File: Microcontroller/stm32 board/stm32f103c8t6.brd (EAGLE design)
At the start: 100 x 80 mm, 19 parts, among them J2 796136-1, Q1 8MHz, U1 STM32F103C8T6, X1 32.768KHZ

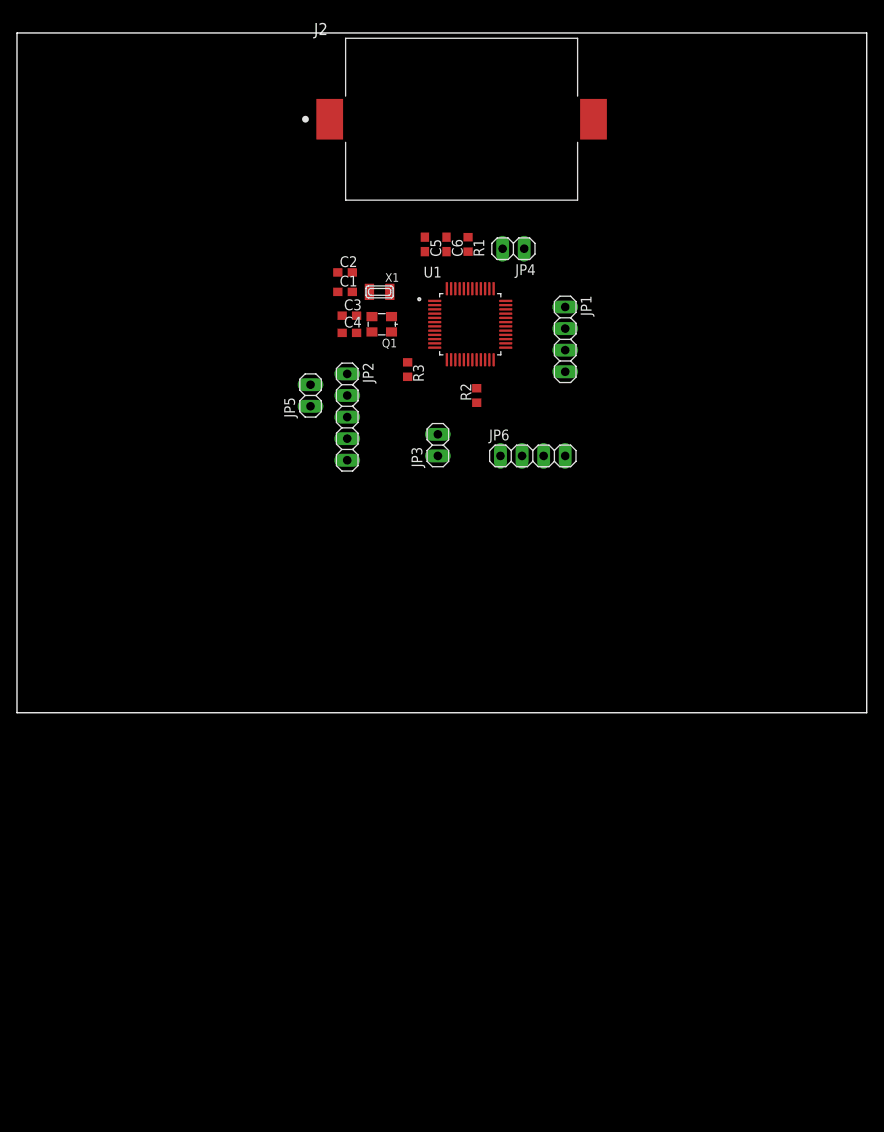
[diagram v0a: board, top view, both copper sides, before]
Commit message: added new stm board
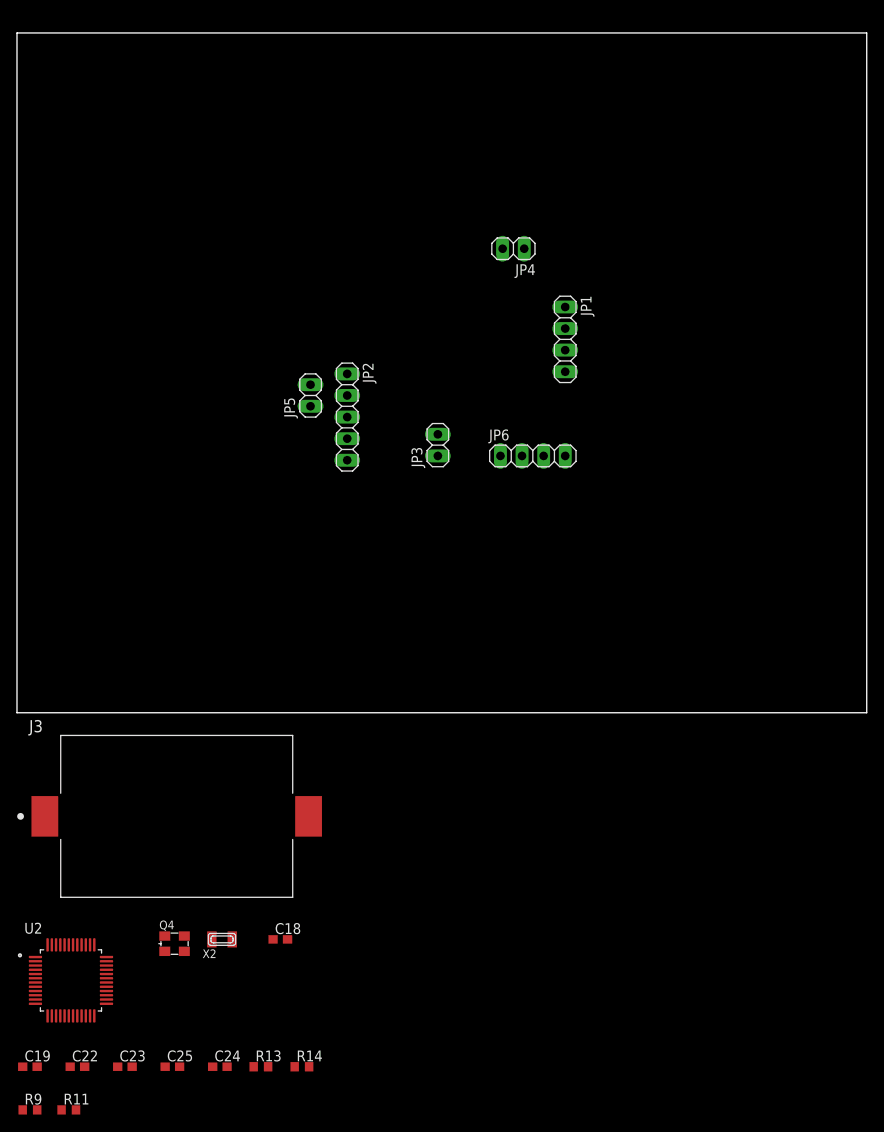
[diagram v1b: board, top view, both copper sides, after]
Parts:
- removed C1, C2: 15pF, rcl:C0603
- removed C3, C4: 22pF, rcl:C0603
- removed C5: 1uF, rcl:C0603
- removed C6: 10nF, rcl:C0603
- removed J2: 796136-1, 796136-1:TE_796136-1
- removed Q1: 8MHz, crystal-geyer_V1_0:3.2X2.5_KX-7
- removed R1, R2, R3: 10K, rcl:R0603
- removed U1: STM32F103C8T6, STM32F103C8T6:QFP50P900X900X160-48N
- removed X1: 32.768KHZ, adafruit:XTAL3215
- added C18, C19: 15pF, rcl:C0603
- added C22, C23: 22pF, rcl:C0603
- added C24: 1uF, rcl:C0603
- added C25: 10nF, rcl:C0603
- added J3: 796136-1, 796136-1:TE_796136-1
- added Q4: 8MHz, crystal-geyer_V1_0:3.2X2.5_KX-7
- added R11, R13, R9: 10K, rcl:R0603
- added R14: 1M, rcl:R0603
- added U2: STM32F103C8T6, STM32F103C8T6:QFP50P900X900X160-48N
- added X2: 32.768KHZ, adafruit:XTAL3215
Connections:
- removed net JTDO: U1.39
- removed net JTRST: U1.40
- removed net N$1: C1.2, U1.3, X1.P$2
- removed net N$11: U1.18
- removed net N$12: U1.19
- removed net N$13: U1.13
- removed net N$14: U1.14
- removed net N$15: U1.41
- removed net N$16: U1.42
- removed net N$17: U1.43
- removed net N$18: U1.45
- removed net N$19: U1.46
- removed net N$2: C2.2, U1.4, X1.P$1
- removed net N$20: U1.21
- removed net N$21: U1.22
- removed net N$22: U1.25
- removed net N$23: U1.26
- removed net N$24: U1.27
- removed net N$25: U1.28
- removed net N$26: U1.15
- removed net N$27: U1.16
- removed net N$28: U1.17
- removed net N$29: U1.29
- removed net N$3: C4.2, Q1.3, U1.6
- removed net N$4: C3.2, Q1.1, U1.5
- removed net N$5: J2.1, U1.1
- removed net N$6: U1.10
- removed net N$7: U1.11
- removed net N$8: U1.12
- new net A1: U2.2
- new net BUTTON_1: U2.19
- new net CSN_RF: U2.43
- new net CS_FLASH: U2.29
- new net CS_RF: U2.42
- new net D+/RF_IRQ: U2.33
- new net ESP_RESET_PIN: U2.18
- new net N$10: C19.2, U2.4, X2.P$1
- new net N$30: C23.2, Q4.3, R14.1, U2.6
- new net N$31: C22.2, Q4.1, R14.2, U2.45, U2.5
- new net N$32: J3.1, U2.1, U2.46
- new net N$40: U2.10
- new net N$41: U2.11
- new net N$42: U2.12
- new net N$43: U2.13
- new net N$9: C18.2, U2.3, X2.P$2
- new net NETWORK: U2.15
- new net PIPE_RX: U2.22
- new net PIPE_TX: U2.21
- new net RF_LED: U2.14
- new net SERVER_LED: U2.16
- new net SPI11_MISO1: U2.40
- new net SPI11_MOSI1: U2.41
- new net SPI11_SCLK1: U2.39
- new net SPI2_MISO2: U2.27
- new net SPI2_MOSI2: U2.28
- new net SPI2_SCLK2: U2.26
- new net SPI2_SS2: U2.25
- new net WIFI_LED: U2.17
- net BOOT0: now also R9.2, U2.44; no longer R1.2, U1.44
- net BOOT1: now also R11.2, U2.20; no longer R2.2, U1.20
- net D+: no longer U1.33
- net D-: now also U2.32; no longer U1.32
- net GND: now also C18.1, C19.1, C22.1, C23.1, C24.1, C25.1, J3.2, R11.1, R9.1, U2.23, U2.35, U2.47, U2.8; no longer C1.1, C2.1, C3.1, C4.1, C5.1, C6.1, J2.2, R1.1, R2.1, U1.23, U1.35, U1.47, U1.8
- net JTCL/SWCLK: now also U2.37; no longer U1.37
- net JTDI: now also U2.38; no longer U1.38
- net JTMS/SWDIO: now also U2.34; no longer U1.34
- net NRST: now also R13.1, U2.7; no longer R3.1, U1.7
- net RX1: now also U2.31; no longer U1.31
- net TX1: now also U2.30; no longer U1.30
- net VCC: now also C24.2, C25.2, R13.2, U2.24, U2.36, U2.48, U2.9; no longer C5.2, C6.2, R3.2, U1.24, U1.36, U1.48, U1.9
